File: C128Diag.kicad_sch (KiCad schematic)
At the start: 60 parts, among them J1 CP1, J2 CP2, J3 KB, J4 Cas, J5 Vid, J6 Serial, J7 UP, P1 1k, U1 4066, U10 74LS04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

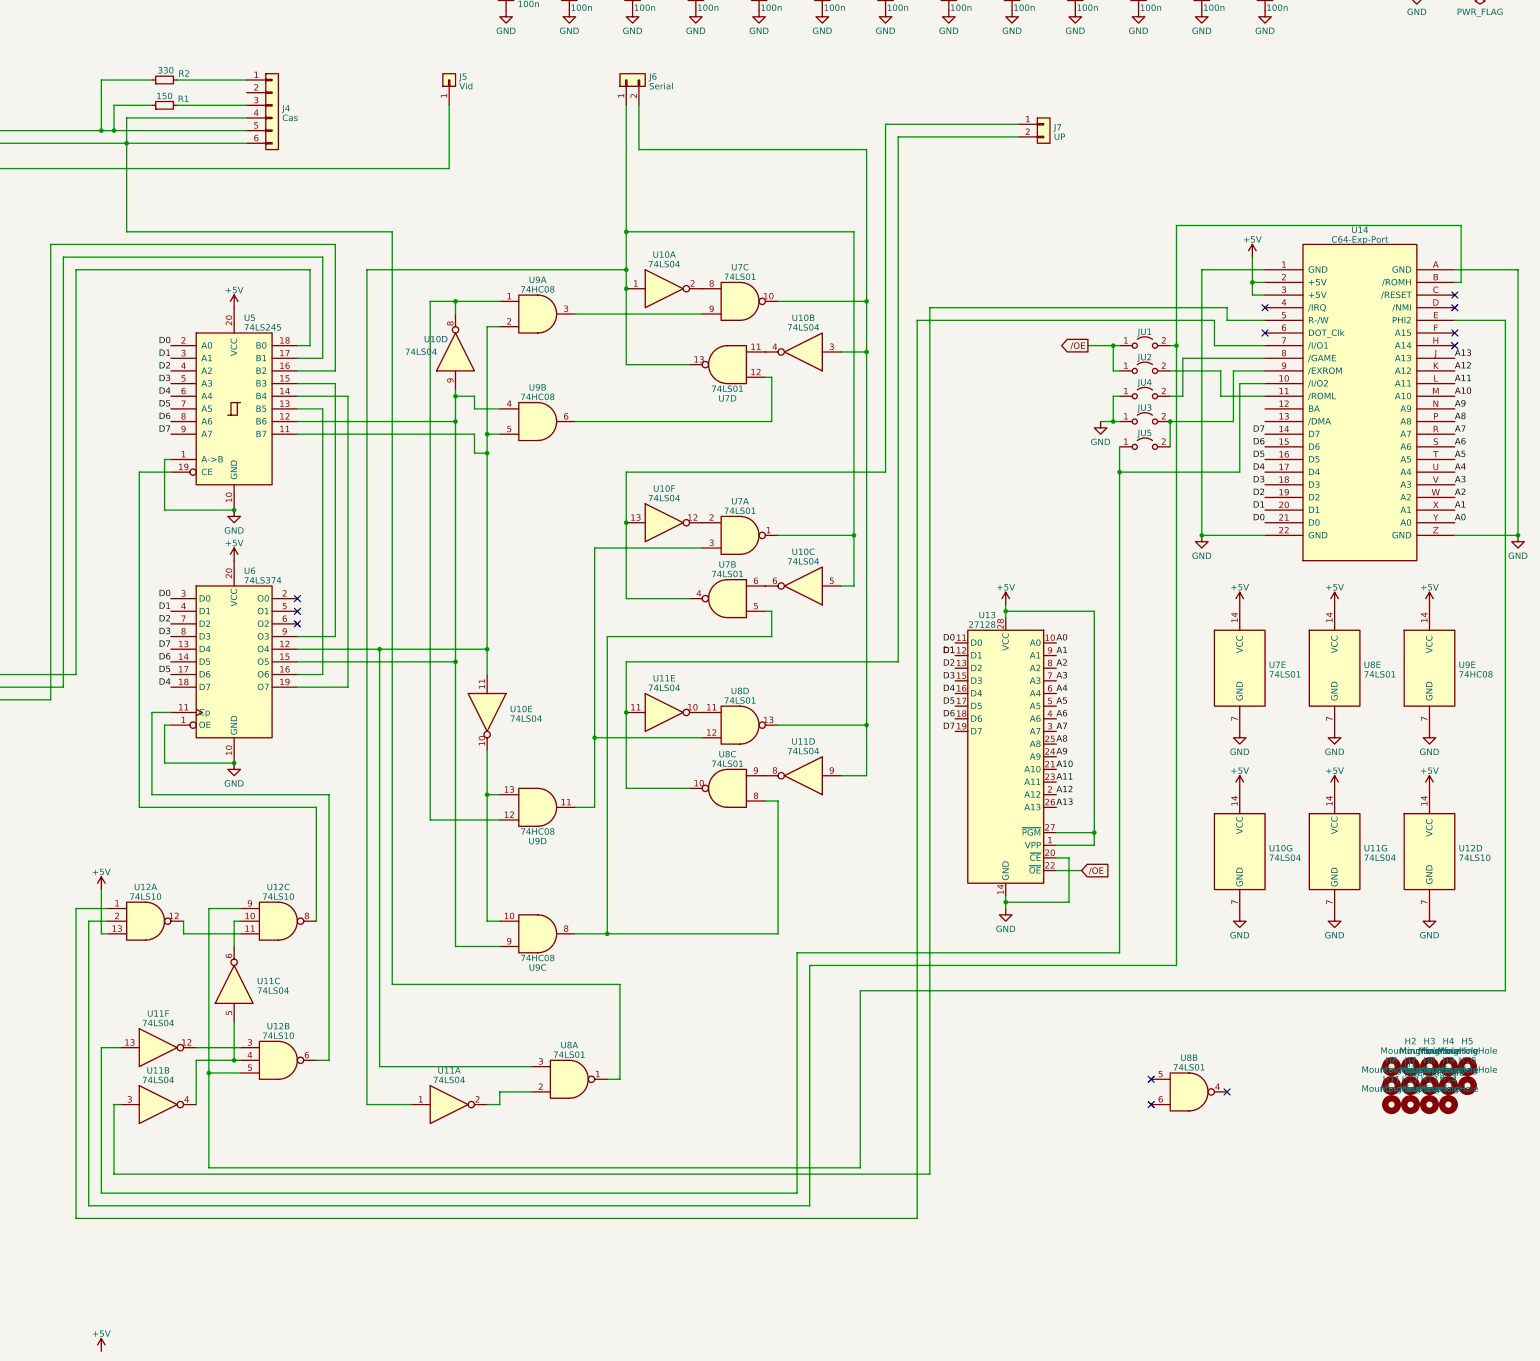
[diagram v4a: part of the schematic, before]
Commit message: Tracing traces and reconstructing schematics, might be complete.
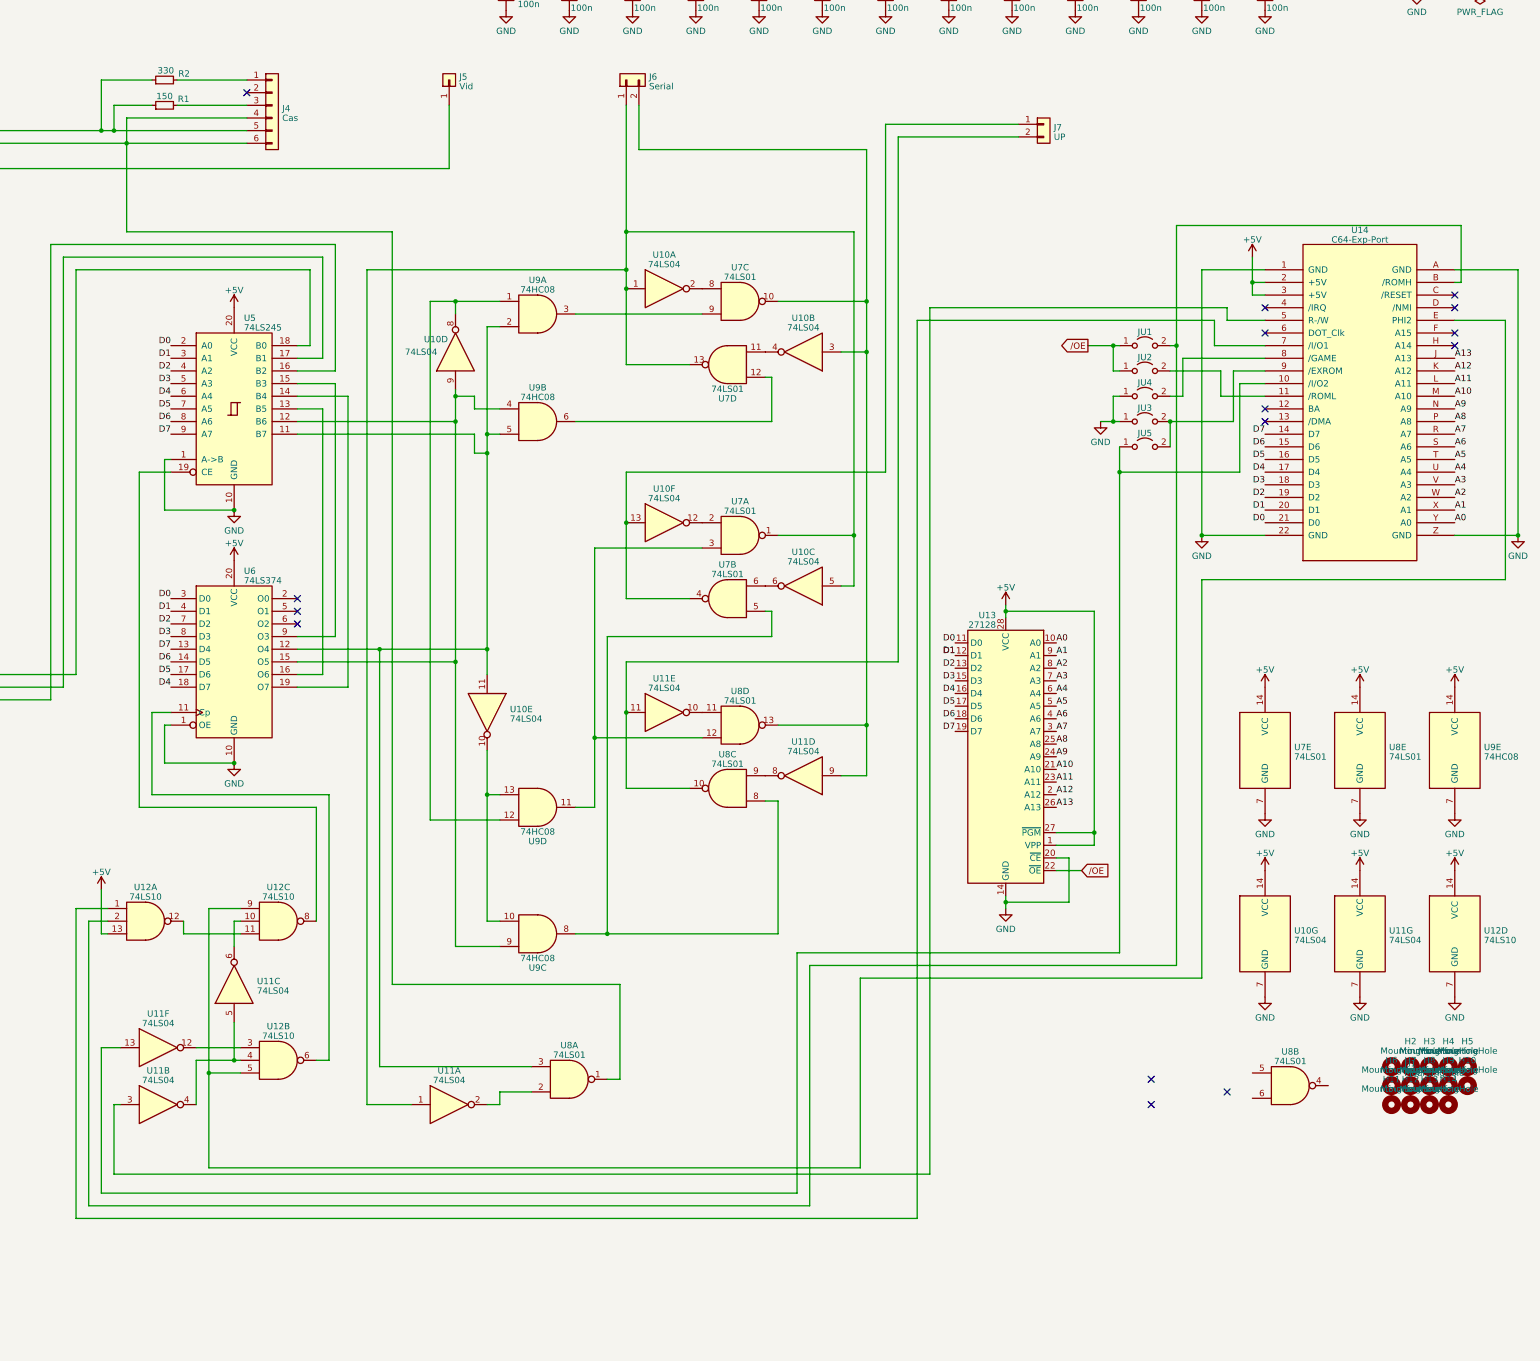
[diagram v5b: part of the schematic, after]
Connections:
- no-connect marks 12 -> 15
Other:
- company: (none) -> www.hackup.net
- title: (none) -> C128Diag
- moved on the sheet: U10G, U11G, U12D, U7E, U8B, U8E, U9E

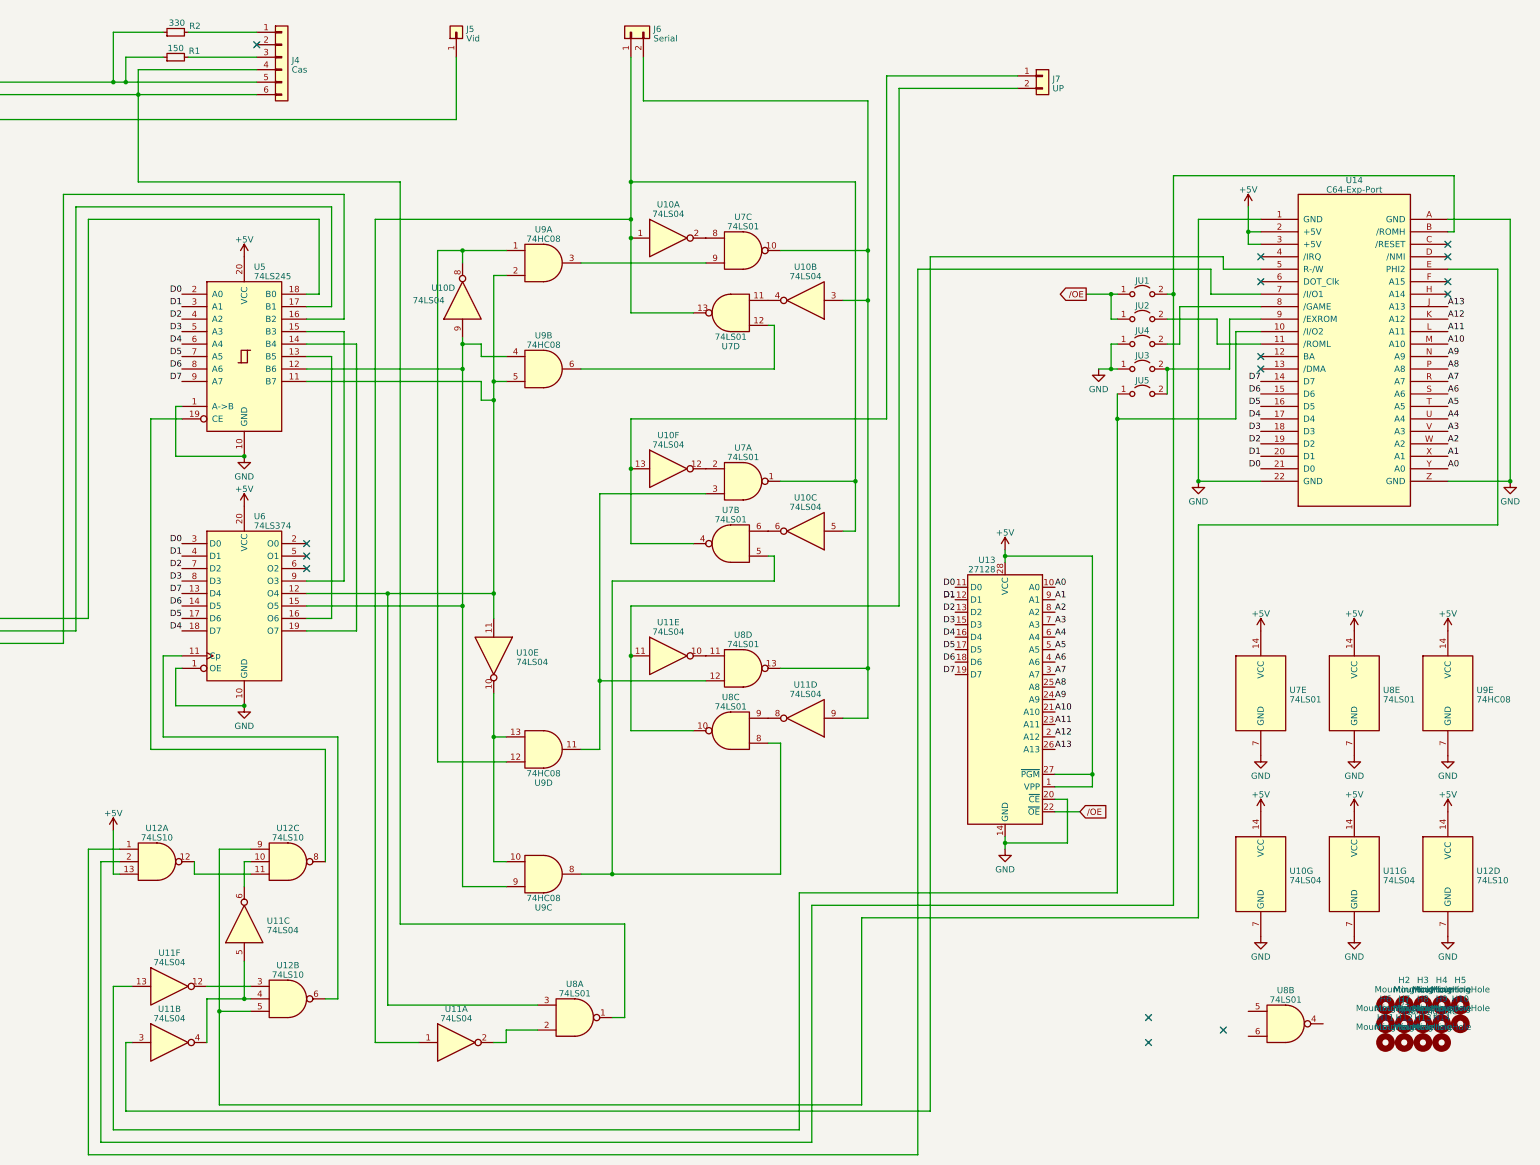
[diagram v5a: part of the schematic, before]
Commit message: Cleaning up schematics.
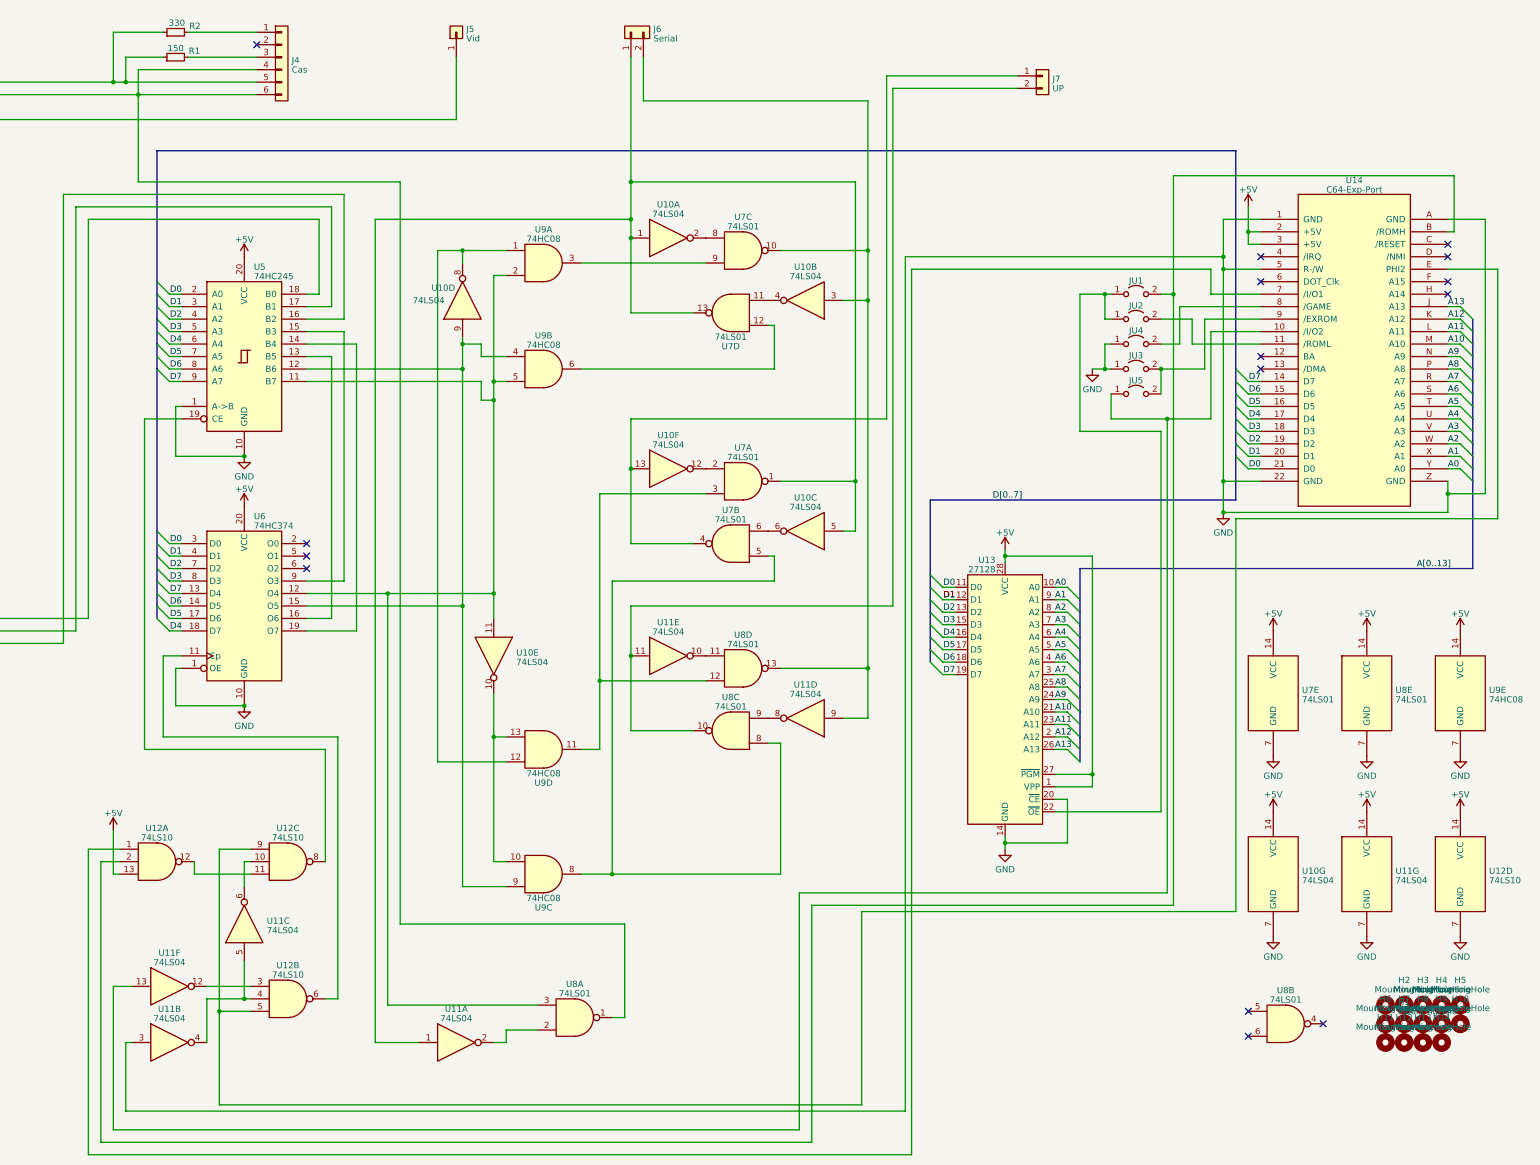
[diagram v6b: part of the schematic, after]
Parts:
- U5: value 74LS245 -> 74HC245
- U6: value 74LS374 -> 74HC374
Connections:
- net GND: now also U11.3, U14.5 (R-/W)
- net /OE: no longer names the net of JU1.1 (A), JU2.1 (A), U13.22 (~{OE})
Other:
- moved on the sheet: JU1, JU2, JU3, JU4, JU5, U10G, U11G, U12D, U7E, U8E, U9E

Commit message: Cleaning up schematics.
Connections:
- net GND: no longer U11.3, U14.5 (R-/W)
- new net: U11.3, U14.5 (R-/W)
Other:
- moved on the sheet: C1, C10, C11, C12, C13, C14, C15, C2, C3, C4, C5, C6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

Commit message: Cleaning up board layout.
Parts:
- R1, R2, R3, R4: footprint Resistor_THT:R_Axial_DIN0309_L9.0mm_D3.2mm_P12.70mm_Horizontal -> C128Diag:R_Axial_P12.70mm_Horizontal
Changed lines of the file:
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@@
   (title_block
     (title "C128Diag")
+    (date "2023-05-04")
     (rev "0")
     (company "www.hackup.net")
@@
       (effects (font (size 1.27 1.27)) (justify left))
     )
-    (property "Footprint" "Resistor_THT:R_Axial_DIN0309_L9.0mm_D3.2mm_P12.70mm_Horizontal" (at 77.47 223.52 0)
+    (property "Footprint" "C128Diag:R_Axial_P12.70mm_Horizontal" (at 77.47 223.52 0)
       (effects (font (size 1.27 1.27)) hide)
     )
@@
       (effects (font (size 1.27 1.27)) (justify left))
     )
-    (property "Footprint" "Resistor_THT:R_Axial_DIN0309_L9.0mm_D3.2mm_P12.70mm_Horizontal" (at 134.62 19.05 0)
+    (property "Footprint" "C128Diag:R_Axial_P12.70mm_Horizontal" (at 134.62 19.05 0)
       (effects (font (size 1.27 1.27)) hide)
     )
@@
       (effects (font (size 1.27 1.27)))
     )
-    (property "Footprint" "Resistor_THT:R_Axial_DIN0309_L9.0mm_D3.2mm_P12.70mm_Horizontal" (at 134.62 24.13 0)
+    (property "Footprint" "C128Diag:R_Axial_P12.70mm_Horizontal" (at 134.62 24.13 0)
       (effects (font (size 1.27 1.27)) hide)
     )
@@
       (effects (font (size 1.27 1.27)) (justify left))
     )
-    (property "Footprint" "Resistor_THT:R_Axial_DIN0309_L9.0mm_D3.2mm_P12.70mm_Horizontal" (at 77.47 228.6 0)
+    (property "Footprint" "C128Diag:R_Axial_P12.70mm_Horizontal" (at 77.47 228.6 0)
       (effects (font (size 1.27 1.27)) hide)
     )
